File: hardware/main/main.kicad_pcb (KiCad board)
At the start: 4 copper layers, 59.7 x 109.5 mm, 235 parts, among them J101 ST_LINK, J102 USART, J301 Overvoltage_protection, J302 Rad_sensor, J303 Mos_temp, J304 Diode_temp, J601 Supplies, J801 RJ45_Shielded, J802 RJ45_Shielded, Q401 BSC093N15NS5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

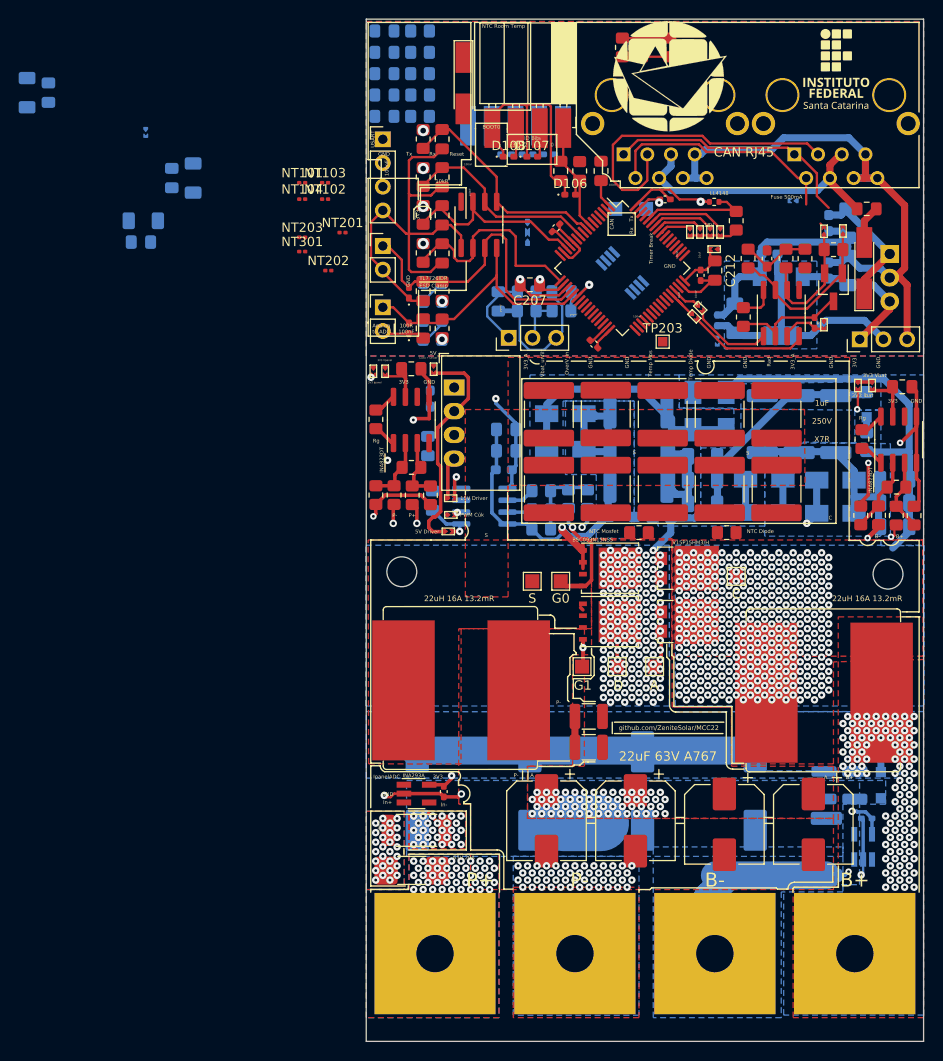
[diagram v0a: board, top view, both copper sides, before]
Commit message: Layout: Finalize first vesion of control (DRC ok) and modify vias for better via density
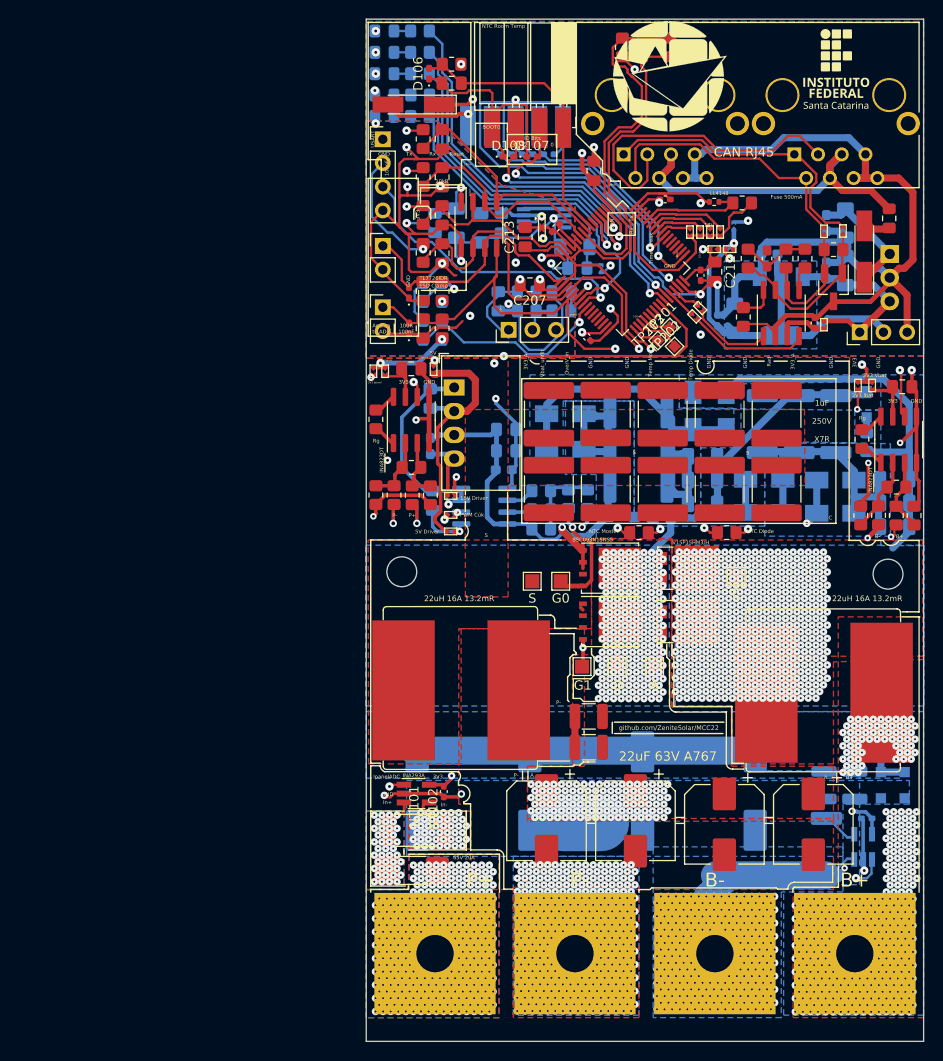
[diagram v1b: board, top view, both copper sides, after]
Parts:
- added C213: 50V 1uF X7R ±10% 0805, Capacitor_SMD:C_0805_2012Metric_Pad1.18x1.45mm_HandSolder, F.Cu at (35.8, 105.9)
- added D414: SMF64A, Diode_SMD:D_SOD-123F, B.Cu at (76.5, 164.6)
- C211: value 50V 100nF X7R ±10% 0402 -> 50V 10nF X7R ±10% 0402
- C309, C310, C311, C312: value 50V 100nF 0805 -> ?
- D102: value LL4148 -> BYD77
- JP101, JP203: moved to F.Cu
- NT101, NT102, NT301: footprint Resistor_SMD:R_0201_0603Metric -> Zenite:NetTie-2_SMD_Pad0.3mm
- NT103, NT104, NT201, NT202, NT203: footprint Resistor_SMD:R_0201_0603Metric -> Zenite:NetTie-2_SMD_Pad0.3mm; moved to B.Cu
- R318, R319, R320, R321: value 100R 0805 -> ?
- TP201, TP202: footprint TestPoint:TestPoint_Pad_1.5x1.5mm -> Zenite:TestPoint_Pad_1.0x1.0mm_small; moved to F.Cu
- TP203: footprint TestPoint:TestPoint_Pad_1.0x1.0mm -> Zenite:TestPoint_Pad_1.0x1.0mm_small
- U701: value MCP2551 -> MCP2561
- moved NT104 91.8 mm to (70.6, 172.5), turned to 180 degrees
- moved NT103 89.9 mm to (70.6, 170.2), turned to 180 degrees
- moved NT101 67.7 mm to (22.9, 166.9), turned to -90 degrees
- moved NT102 66.1 mm to (24.9, 167.1), turned to -90 degrees
- moved JP103 50.6 mm to (43.9, 108.7), turned to 90 degrees
- moved C313 48.0 mm to (28.4, 104.4)
- moved C202 46.8 mm to (41.4, 109.2)
- moved C201 46.3 mm to (41.1, 106.9)
- moved C314 43.7 mm to (26.2, 104.4)
- moved C203 35.6 mm to (33.3, 104.4)
- moved C204 31.2 mm to (31.0, 104.9)
- moved NT301 29.3 mm to (41.1, 109.2), turned to 90 degrees
- moved NT202 25.1 mm to (39.1, 103.6)
- moved NT203 24.7 mm to (36.6, 104.3), turned to 180 degrees
- moved NT201 23.2 mm to (39.1, 109.2), turned to 180 degrees
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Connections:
- C302 pad 1: /Analog/V_temp_diode -> /Analog/V_temp_mos
- C303 pad 1: /Analog/V_temp_mos -> /Analog/V_temp_diode
- D301 pad 2: /Analog/V_temp_diode -> /Analog/V_temp_mos
- D302 pad 2: /Analog/V_temp_mos -> /Analog/V_temp_diode
- J303 pad 1: /Analog/V_temp_mos -> /Analog/V_temp_diode
- J304 pad 1: /Analog/V_temp_diode -> /Analog/V_temp_mos
- R301 pad 1: /Analog/V_temp_mos -> /Analog/V_temp_diode
- R302 pad 1: /Analog/V_temp_diode -> /Analog/V_temp_mos
- TH301 pad 1: /Analog/V_temp_mos -> /Analog/V_temp_diode
- TH302 pad 1: /Analog/V_temp_diode -> /Analog/V_temp_mos
- TP201 pad 1: Net-(U202-Pad61) -> Net-(TP201-Pad1)
- TP202 pad 1: Net-(U202-Pad62) -> Net-(TP202-Pad1)
- U202 pad 20: /Analog/V_temp_mos -> /Analog/V_temp_diode
- U202 pad 21: /Analog/V_temp_diode -> /Analog/V_temp_mos
- U202 pad 35: unconnected-(U202-Pad35) -> Net-(TP202-Pad1)
- U202 pad 36: unconnected-(U202-Pad36) -> Net-(TP201-Pad1)
- U202 pad 61: Net-(U202-Pad61) -> unconnected-(U202-Pad61)
- U202 pad 62: Net-(U202-Pad62) -> unconnected-(U202-Pad62)
- U305 pad 3: /Analog/V_temp_mos -> /Analog/V_temp_diode
- U305 pad 4: /Analog/V_temp_diode -> /Analog/V_temp_mos
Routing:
- net GNDA: track 368.2 -> 793.9 mm, vias 8 -> 22
- net GND: track 180.9 -> 535.8 mm, vias 2 -> 16
- net Net-(R321-Pad1): track 0.00 -> 138.8 mm, vias 1 -> 2
- net /3V3_Analog: track 21.2 -> 155.5 mm, vias 2 -> 7
- net /STM32/3V3_MCU: track 28.8 -> 105.3 mm, vias 2 -> 7
- net /Analog/V_bat_unfiltered+: track 10.4 -> 83.3 mm, vias 1 -> 2
- net +5V: track 15.8 -> 88.3 mm, vias 0 -> 2
- net Net-(R320-Pad1): track 0.00 -> 67.6 mm, vias 1 -> 2
- net /PWM: track 0.00 -> 50.7 mm, vias 0 -> 2
- net /3V3_STM: track 0.00 -> 48.5 mm, vias 0 -> 2
- net /Analog/V_temp_diode: track 28.0 -> 74.4 mm, vias 0 -> 2
- net /STM32/LED_0: track 0.00 -> 39.9 mm, vias 0 -> 1
- net /STM32/STATUS_LED: track 0.00 -> 37.4 mm, vias 0 -> 1
- net /STM32/Bat_OverV_Out: track 0.00 -> 36.8 mm, vias 0 -> 1
- net /can_connector/CAN_18V: track 30.3 -> 65.2 mm
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- added copper zone on B.Cu, net GNDA
- added copper zone on F.Cu, net GNDA
- added copper zone on In1.Cu, net GNDA
- added copper zone on In2.Cu, net GNDA

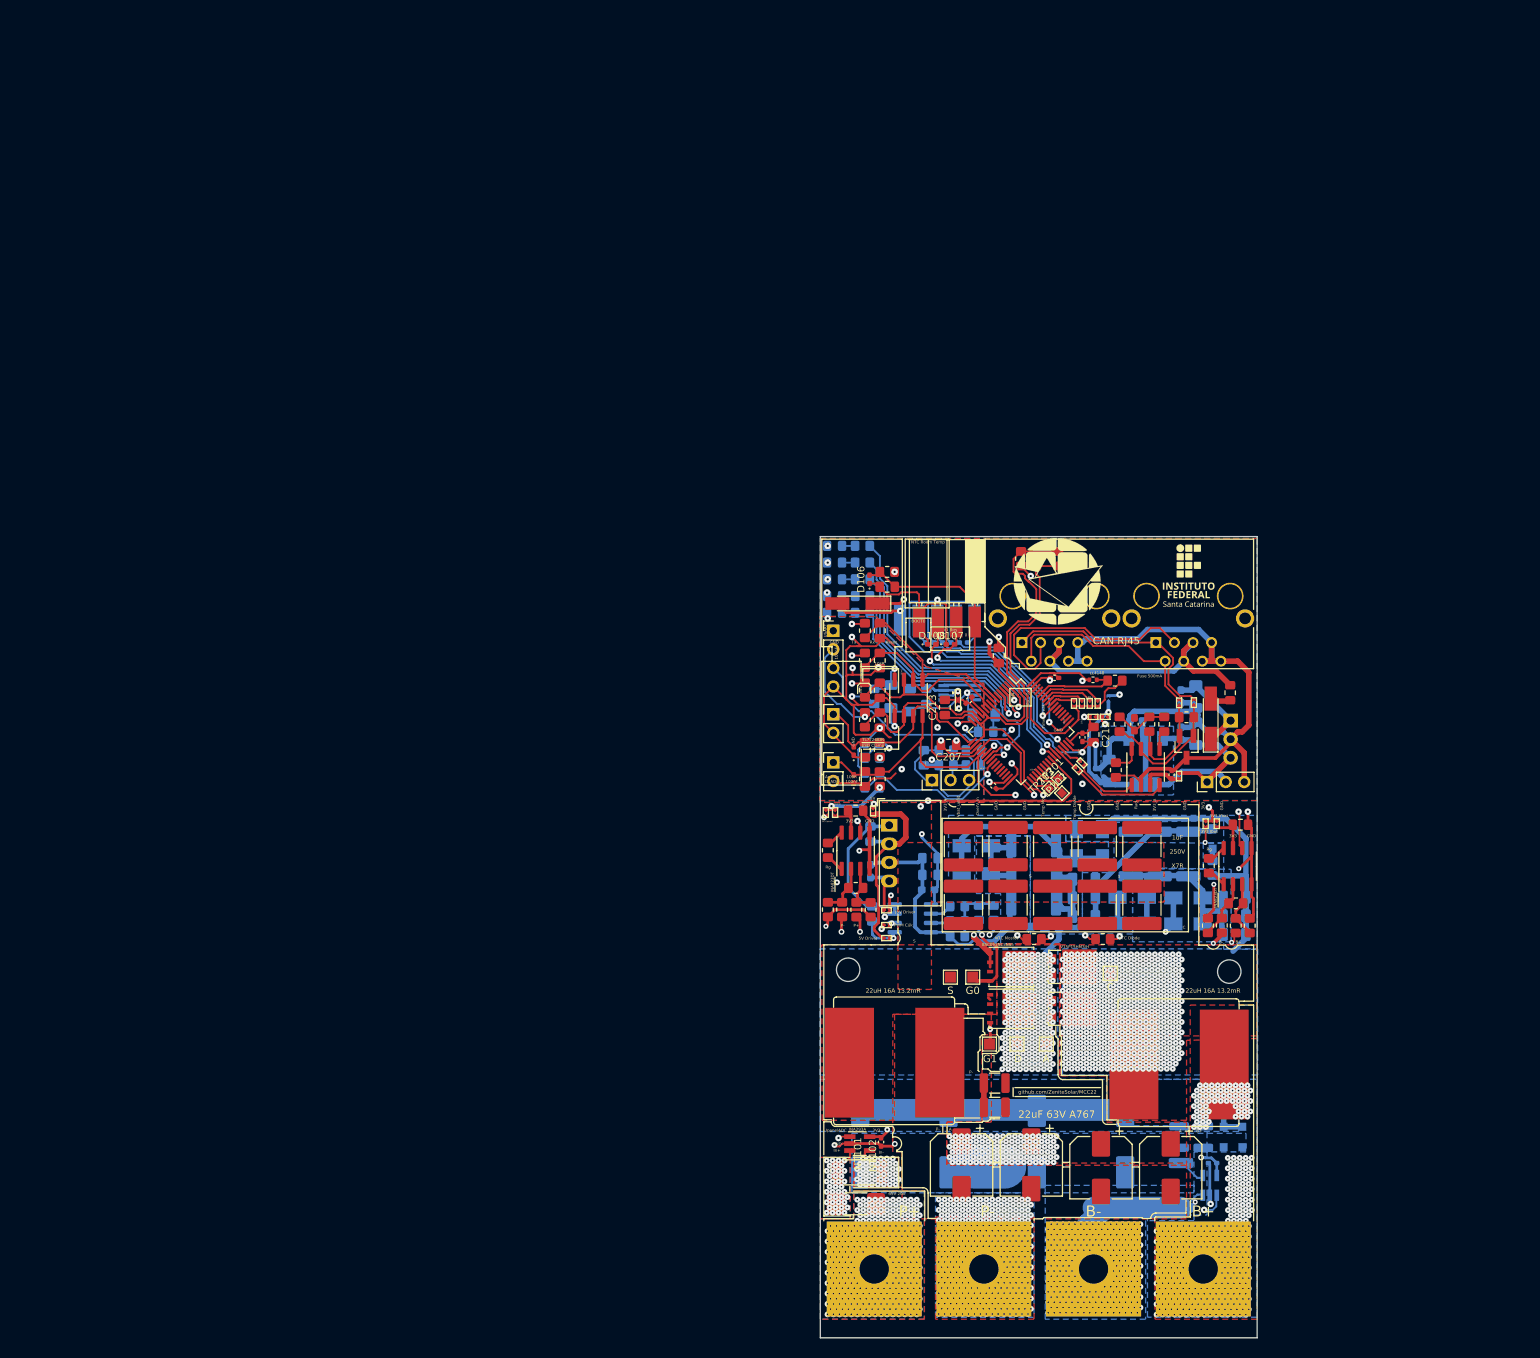
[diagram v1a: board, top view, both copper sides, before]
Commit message: Layout: create margin for mechanical fixation
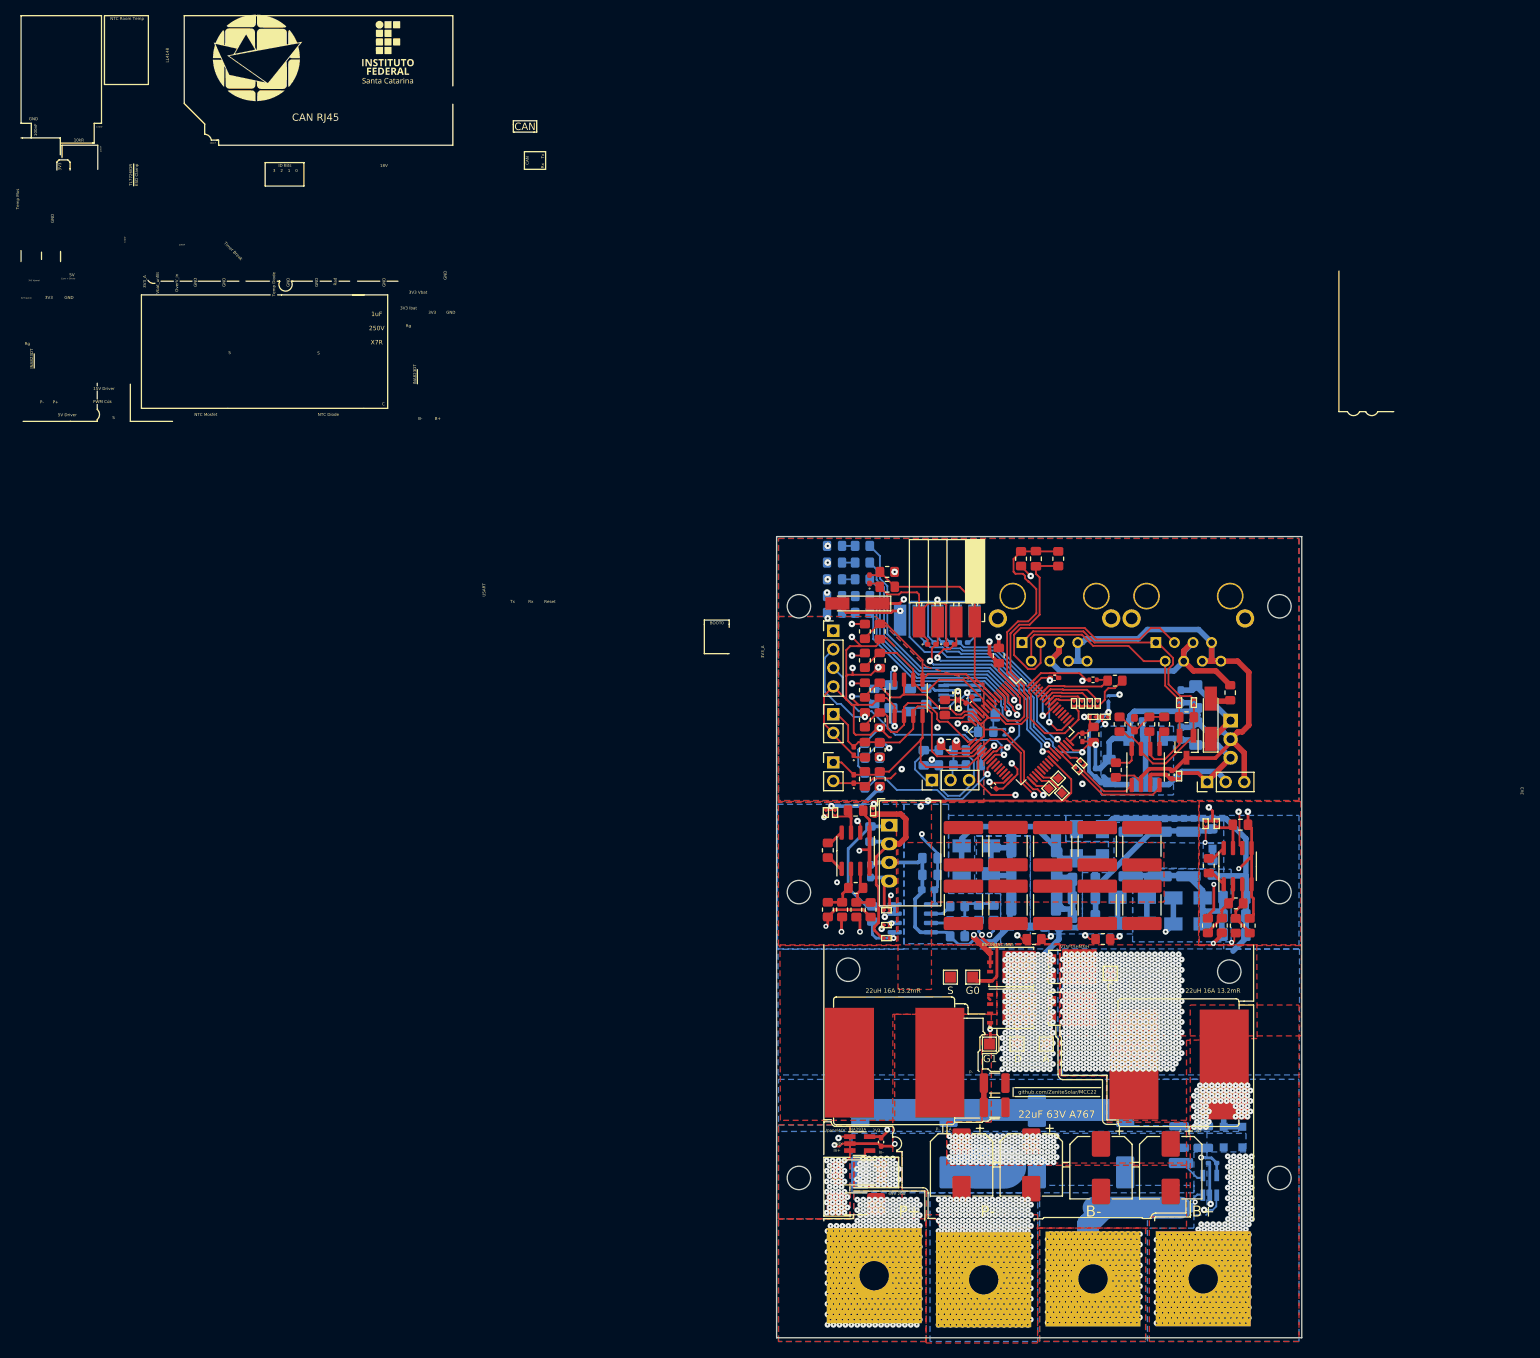
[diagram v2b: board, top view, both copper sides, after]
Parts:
- added ?: , , F.Cu at (15.9, 92.1)
- added ?: , , F.Cu at (81.5, 92.1)
- added ?: , , F.Cu at (81.5, 170.2)
- added ?: , , F.Cu at (15.9, 131.1)
- added ?: , , F.Cu at (81.5, 131.1)
- added ?: , , F.Cu at (15.9, 170.2)
- moved LOGO101 130.7 mm to (-58.1, 17.1)
- moved LOGO102 130.7 mm to (-40.3, 16.4)
- moved LOGO103 92.2 mm to (120.9, 97.9)
- moved LOGO104 92.2 mm to (113.2, 98.2)
- moved LOGO105 92.2 mm to (127.8, 85.8)
- moved H101 1.47 mm to (41.1, 184.1)
- moved H103 1.35 mm to (56.1, 184.0)
- moved H104 1.34 mm to (71.1, 184.0)
- moved H102 0.91 mm to (26.2, 183.5)
- moved C312 0.11 mm to (26.9, 95.5)
- moved R321 0.11 mm to (24.9, 95.5)
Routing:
- net /P-: vias 333 -> 365
- net /P+Unfused: vias 307 -> 339
- net /B+: vias 374 -> 393
- added copper zone on F.Cu, net /B-
- added copper zone on In1.Cu, net /B-
- added copper zone on In2.Cu, net /B-
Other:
- board size 59.7 x 109.5 mm -> 71.8 x 109.5 mm
- board text removed: "100R 100nF"
- board text removed: "Analog to ADC"

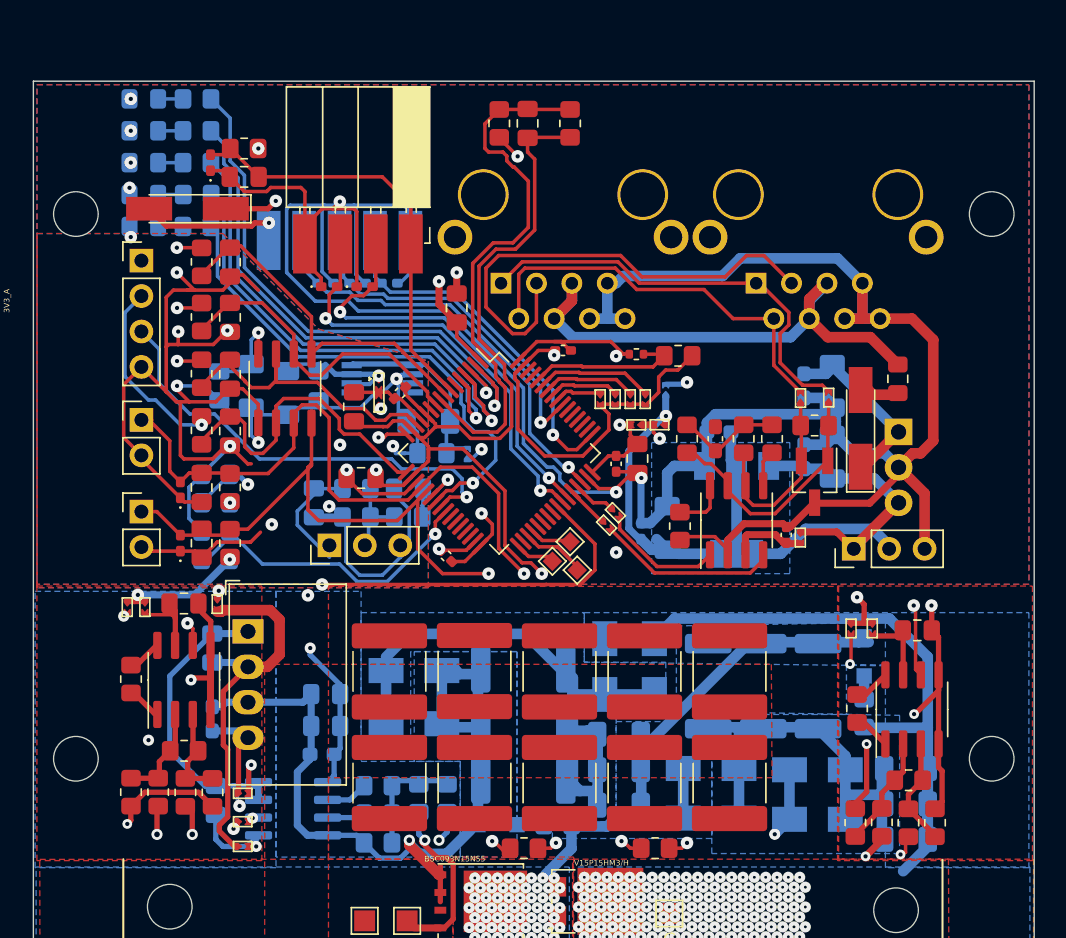
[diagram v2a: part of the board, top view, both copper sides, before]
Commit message: Layout: Update silkscreen
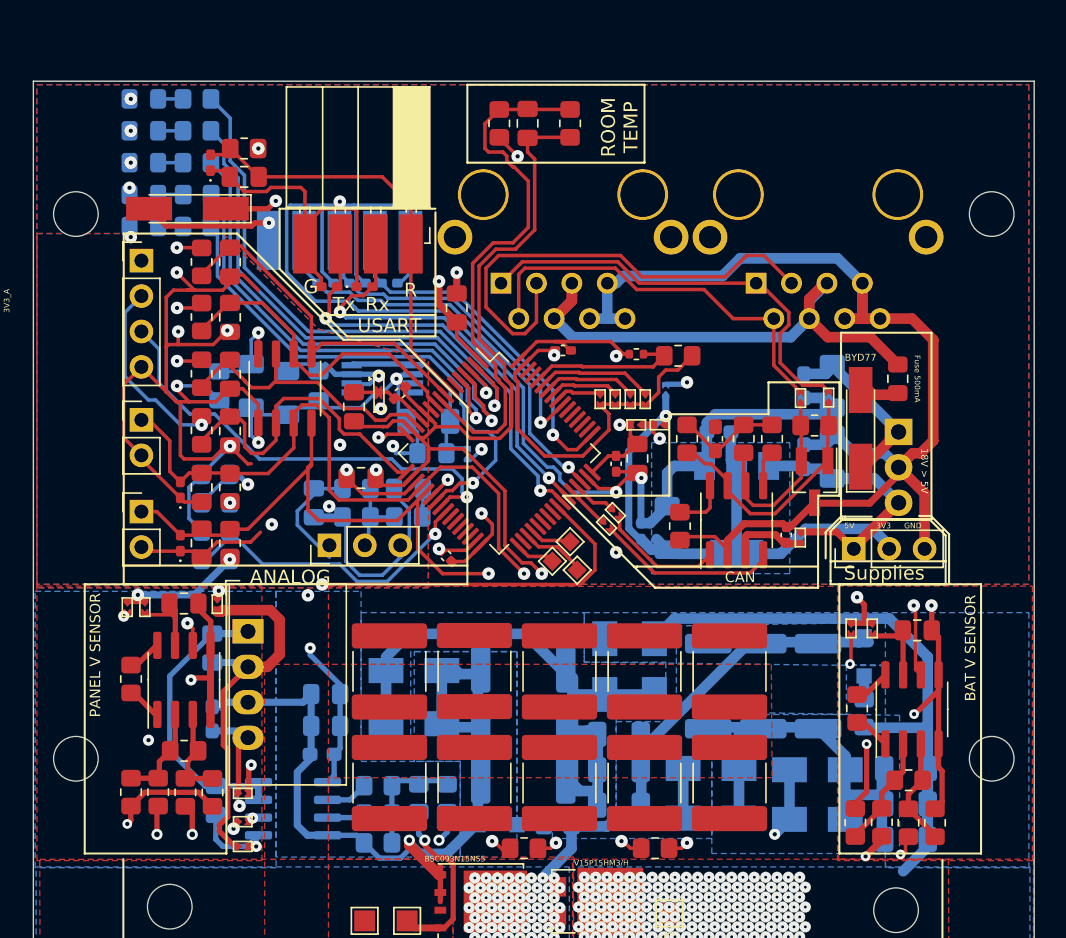
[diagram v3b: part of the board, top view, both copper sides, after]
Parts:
- moved LOGO103 105.0 mm to (16.0, 96.5), turned to -90 degrees
- moved LOGO104 98.4 mm to (15.7, 111.8), turned to -90 degrees
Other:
- board text added: "18V > 5V"
- board text added: "5V > 3.3V"
- board text added: "ANALOG"
- board text added: "BAT V SENSOR"
- board text added: "BYD77"
- board text added: "G"
- board text added: "PANEL V SENSOR"
- board text added: "R"
- board text added: "ROOM TEMP"
- board text added: "SUPPLIES"
